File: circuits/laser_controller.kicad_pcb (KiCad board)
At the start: 4 copper layers, 173 x 61.1 mm, 180 parts, among them J1 USB_MINI_B, J2 USB_MINI_B, J5 24V DC IN, J6 CONN_RJ45, Q1 SOT-23, Q2 SOT-23, Q3 SOT-23, Q4 SOT-23, Q5 SOT-23, Q6 SOT-23, SW1 SW_PUSH, SW2 SW_PUSH, SW3 SW_PUSH, U1 SOIC-8_3.9x4.9mm_P1.27mm, U10 QFN-28-1EP_5x5mm_P0.5mm_EP3.3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, U11 SOT-23-5, U12 TSSOP-14_4.4x5mm_P0.65mm, U13 SOT-23, U14 LQFP-64_10x10mm_P0.5mm, U15 TSOT-23-6, U16 TSOT-23-6, U2 SOIC-8_3.9x4.9mm_P1.27mm, U3 SOIC-8_3.9x4.9mm_P1.27mm, U4 SOIC-8_3.9x4.9mm_P1.27mm, U5 SOT-23-5, U6 SOT-23-5, U7 SOT-23-5, U8 SOT-23-5, U9 ESP32-S3-WROOM-1

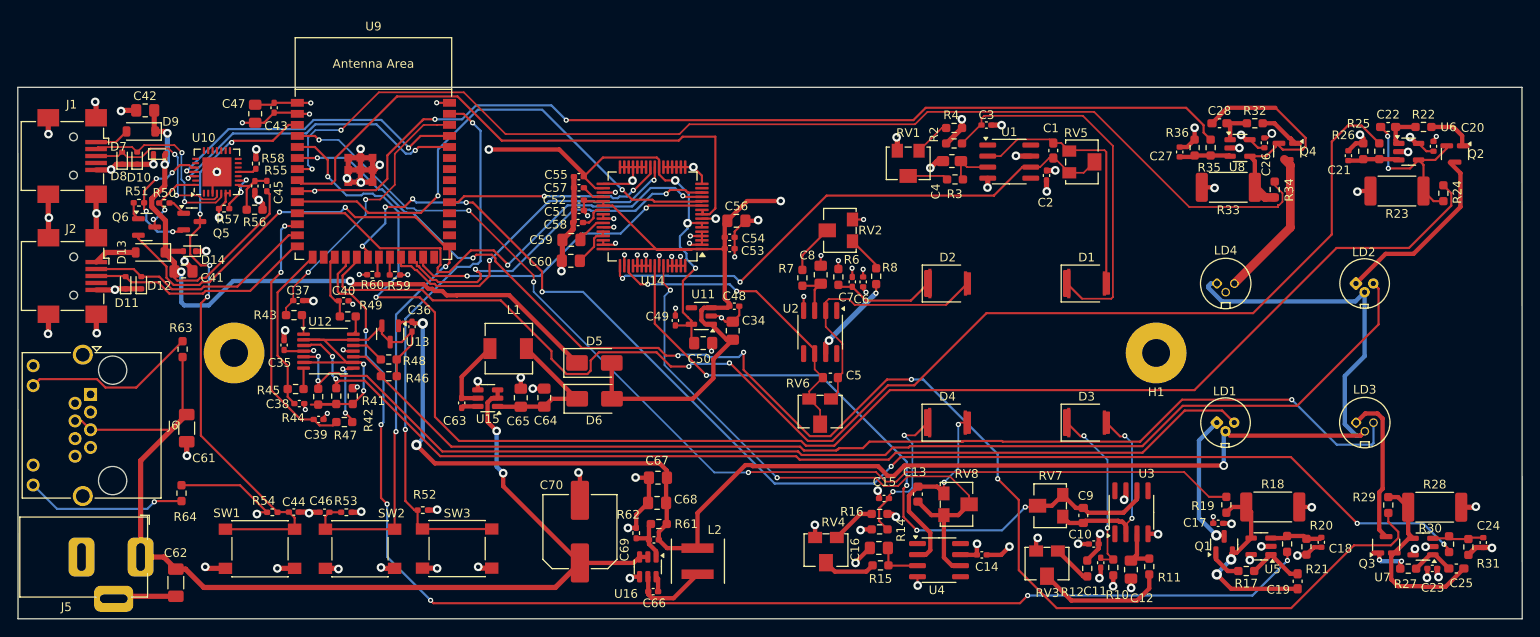
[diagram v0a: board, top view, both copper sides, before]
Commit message: Label laser controller board sections
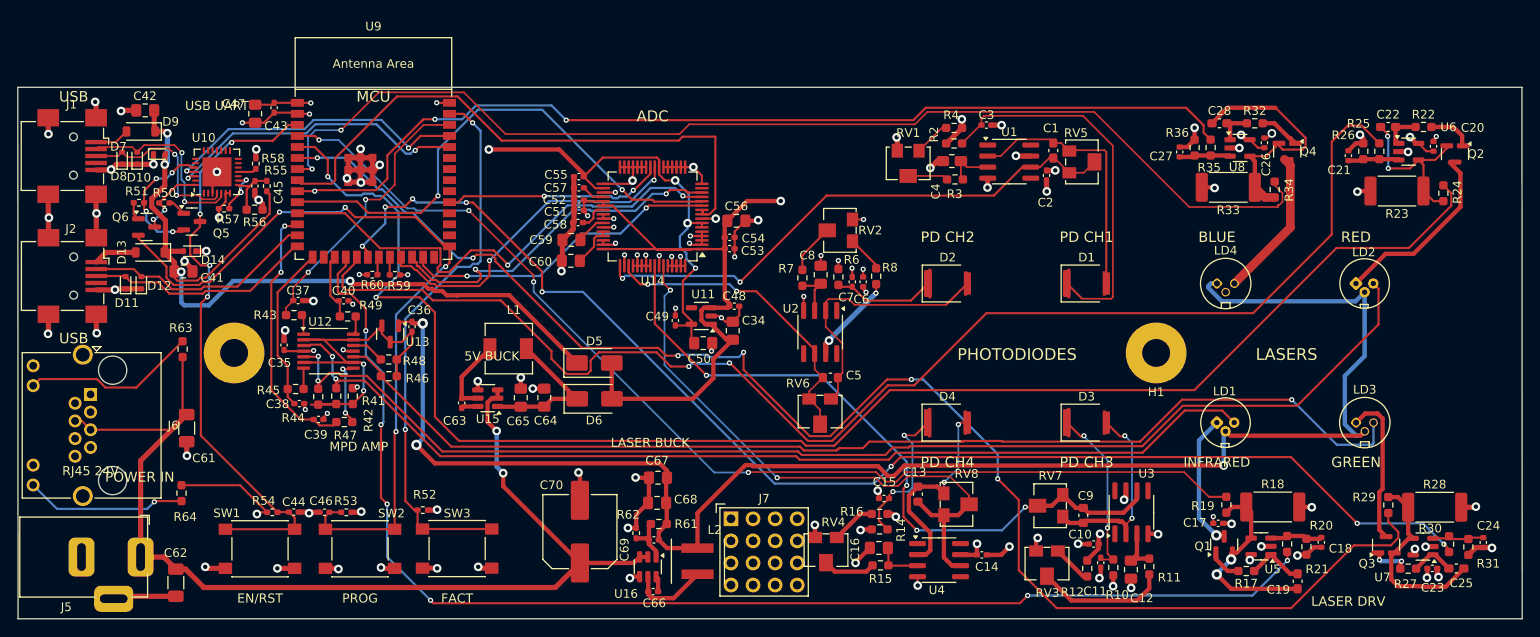
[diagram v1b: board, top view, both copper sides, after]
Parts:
- added J7: UTILITY_4X4, PinHeader_4x04_P2.54mm_Vertical, F.Cu at (113.0, 129.5)
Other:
- board text added: "5V BUCK"
- board text added: "ADC"
- board text added: "BLUE"
- board text added: "EN/RST"
- board text added: "FACT"
- board text added: "GREEN"
- board text added: "INFRARED"
- board text added: "LASER BUCK"
- board text added: "LASER DRV"
- board text added: "LASERS"
- board text added: "MCU"
- board text added: "MPD AMP"
- board text added: "PD CH1"
- board text added: "PD CH2"
- board text added: "PD CH3"
- board text added: "PD CH4"
- board text added: "PHOTODIODES"
- board text added: "POWER IN"
- board text added: "PROG"
- board text added: "RED"
- board text added: "RJ45 24V"
- board text added: "USB"
- board text added: "USB UART"
- board text added: "vivonics"
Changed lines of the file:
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@@
+    )
+  )
+  (footprint "PinHeader_4x04_P2.54mm_Vertical" (layer "F.Cu")
+    (at 113 129.5)
+    (descr "Through hole straight pin header, 4x04, 2.54mm pitch, vertical")
+    (tags "Through hole pin header THT 4x04 2.54mm vertical")
+    (attr through_hole)
+    (fp_text reference "J7" (at 3.81 -2.33) (layer "F.SilkS")
+        (effects (font (size 1 1) (thickness 0.15)))
+    )
+    (fp_text value "UTILITY_4X4" (at 3.81 9.95) (layer "F.Fab")
+        (effects (font (size 1 1) (thickness 0.15)))
+    )
+    (fp_text user "${REFERENCE}" (at 3.81 3.81) (layer "F.Fab")
+        (effects (font (size 1 1) (thickness 0.15)))
+    )
+    (fp_line (start -1.27 -1.27) (end 8.89 -1.27)
+      (stroke (width 0.12) (type solid)) (layer "F.SilkS"))
+    (fp_line (start -1.27 -1.27) (end -1.27 8.89)
+      (stroke (width 0.12) (type solid)) (layer "F.SilkS"))
+    (fp_line (start -1.27 8.89) (end 8.89 8.89)
+      (stroke (width 0.12) (type solid)) (layer "F.SilkS"))
+    (fp_line (start 8.89 -1.27) (end 8.89 8.89)
+      (stroke (width 0.12) (type solid)) (layer "F.SilkS"))
+    (fp_line (start -1.7 -1.7) (end -0.7 -1.7)
+      (stroke (width 0.12) (type solid)) (layer "F.SilkS"))
+    (fp_line (start -1.7 -1.7) (end -1.7 -0.7)
+      (stroke (width 0.12) (type solid)) (layer "F.SilkS"))
+    (fp_line (start -1.8 -1.8) (end 9.42 -1.8)
+      (stroke (width 0.05) (type solid)) (layer "F.CrtYd"))
+    (fp_line (start -1.8 9.42) (end -1.8 -1.8)
+      (stroke (width 0.05) (type solid)) (layer "F.CrtYd"))
+    (fp_line (start 9.42 -1.8) (end 9.42 9.42)
+      (stroke (width 0.05) (type solid)) (layer "F.CrtYd"))
+    (fp_line (start 9.42 9.42) (end -1.8 9.42)
+      (stroke (width 0.05) (type solid)) (layer "F.CrtYd"))
+    (fp_line (start -1.27 -0.27) (end -0.27 -1.27)
+      (stroke (width 0.1) (type solid)) (layer "F.Fab"))
+    (fp_line (start -1.27 -0.27) (end -1.27 8.89)
+      (stroke (width 0.1) (type solid)) (layer "F.Fab"))
+    (fp_line (start -1.27 8.89) (end 8.89 8.89)
+      (stroke (width 0.1) (type solid)) (layer "F.Fab"))
+    (fp_line (start -0.27 -1.27) (end 8.89 -1.27)
+      (stroke (width 0.1) (type solid)) (layer "F.Fab"))
+    (fp_line (start 8.89 -1.27) (end 8.89 8.89)
+      (stroke (width 0.1) (type solid)) (layer "F.Fab"))
+    (pad "1" thru_hole rect (at 0 0) (size 1.7 1.7) (drill 1) (layers "*.Cu" "*.Mask")
+      (net 46 "GND"))
+    (pad "2" thru_hole circle (at 2.54 0) (size 1.7 1.7) (drill 1) (layers "*.Cu" "*.Mask")
+      (net 115 "VIN_24V"))
+    (pad "3" thru_hole circle (at 5.08 0) (size 1.7 1.7) (drill 1) (layers "*.Cu" "*.Mask")
+      (net 2 "+5V"))
+    (pad "4" thru_hole circle (at 7.62 0) (size 1.7 1.7) (drill 1) (layers "*.Cu" "*.Mask")
+      (net 1 "+3V3"))
+    (pad "5" thru_hole circle (at 0 2.54) (size 1.7 1.7) (drill 1) (layers "*.Cu" "*.Mask")
+      (net 110 "PWM1"))
+    (pad "6" thru_hole circle (at 2.54 2.54) (size 1.7 1.7) (drill 1) (layers "*.Cu" "*.Mask")
+      (net 111 "PWM2"))
+    (pad "7" thru_hole circle (at 5.08 2.54) (size 1.7 1.7) (drill 1) (layers "*.Cu" "*.Mask")
+      (net 112 "PWM3"))
+    (pad "8" thru_hole circle (at 7.62 2.54) (size 1.7 1.7) (drill 1) (layers "*.Cu" "*.Mask")
+      (net 113 "PWM4"))
+    (pad "9" thru_hole circle (at 0 5.08) (size 1.7 1.7) (drill 1) (layers "*.Cu" "*.Mask")
+      (net 56 "MPD1"))
+    (pad "10" thru_hole circle (at 2.54 5.08) (size 1.7 1.7) (drill 1) (layers "*.Cu" "*.Mask")
+      (net 57 "MPD2"))
+    (pad "11" thru_hole circle (at 5.08 5.08) (size 1.7 1.7) (drill 1) (layers "*.Cu" "*.Mask")
+      (net 58 "MPD3"))
+    (pad "12" thru_hole circle (at 7.62 5.08) (size 1.7 1.7) (drill 1) (layers "*.Cu" "*.Mask")
+      (net 59 "MPD4"))
+    (pad "13" thru_hole circle (at 0 7.62) (size 1.7 1.7) (drill 1) (layers "*.Cu" "*.Mask")
+      (net 45 "CONVST"))
+    (pad "14" thru_hole circle (at 2.54 7.62) (size 1.7 1.7) (drill 1) (layers "*.Cu" "*.Mask")
+      (net 39 "ADC_BUSY"))
+    (pad "15" thru_hole circle (at 5.08 7.62) (size 1.7 1.7) (drill 1) (layers "*.Cu" "*.Mask")
+      (net 14 "/MCU_ESP32-S3/EN"))
+    (pad "16" thru_hole circle (at 7.62 7.62) (size 1.7 1.7) (drill 1) (layers "*.Cu" "*.Mask")
+      (net 31 "/MCU_ESP32-S3/PROG"))
+    (model "${KIPRJMOD}/packages3d/Connector_PinHeader.3dshapes/PinHeader_4x04_P2.54mm_Vertical.step"
+      (offset (xyz 0 0 0))
+      (scale (xyz 1 1 1))
+      (rotate (xyz 0 0 0))
     )
   )
@@
     (effects (font (size 1.2 1.2) (thickness 0.18)))
   )
+  (gr_text "PD CH2" (at 137.925 97.1 0) (layer "F.SilkS")
+    (effects (font (size 1.2 1.2) (thickness 0.18)))
+  )
+  (gr_text "PD CH1" (at 153.9 97.1 0) (layer "F.SilkS")
+    (effects (font (size 1.2 1.2) (thickness 0.18)))
+  )
+  (gr_text "BLUE" (at 168.9 97.1 0) (layer "F.SilkS")
+    (effects (font (size 1.2 1.2) (thickness 0.18)))
+  )
+  (gr_text "RED" (at 184.88 97.1 0) (layer "F.SilkS")
+    (effects (font (size 1.2 1.2) (thickness 0.18)))
+  )
+  (gr_text "PD CH4" (at 137.9 123 0) (layer "F.SilkS")
+    (effects (font (size 1.2 1.2) (thickness 0.18)))
+  )
+  (gr_text "PD CH3" (at 153.9 123 0) (layer "F.SilkS")
+    (effects (font (size 1.2 1.2) (thickness 0.18)))
+  )
+  (gr_text "INFRARED" (at 168.88 123 0) (layer "F.SilkS")
+    (effects (font (size 1.1 1.1) (thickness 0.17)))
+  )
+  (gr_text "GREEN" (at 184.9 123 0) (layer "F.SilkS")
+    (effects (font (size 1.2 1.2) (thickness 0.18)))
+  )
+  (gr_text "PHOTODIODES" (at 145.9 110.6 0) (layer "F.SilkS")
+    (effects (font (size 1.35 1.35) (thickness 0.22)))
+  )
+  (gr_text "LASERS" (at 176.9 110.6 0) (layer "F.SilkS")
+    (effects (font (size 1.35 1.35) (thickness 0.22)))
+  )
+  (gr_text "EN/RST" (at 58.8325 138.65 0) (layer "F.SilkS")
+    (effects (font (size 1.05 1.05) (thickness 0.16)))
+  )
+  (gr_text "PROG" (at 70.3325 138.65 0) (layer "F.SilkS")
+    (effects (font (size 1.05 1.05) (thickness 0.16)))
+  )
+  (gr_text "FACT" (at 81.5025 138.65 0) (layer "F.SilkS")
+    (effects (font (size 1.05 1.05) (thickness 0.16)))
+  )
+  (gr_text "USB" (at 37.4 80.95 0) (layer "F.SilkS")
+    (effects (font (size 1.2 1.2) (thickness 0.18)))
+  )
+  (gr_text "USB" (at 37.4 108.75 0) (layer "F.SilkS")
+    (effects (font (size 1.2 1.2) (thickness 0.18)))
+  )
+  (gr_text "RJ45 24V" (at 39.34 124 0) (layer "F.SilkS")
+    (effects (font (size 1.05 1.05) (thickness 0.16)))
+  )
+  (gr_text "POWER IN" (at 45 124.7 0) (layer "F.SilkS")
+    (effects (font (size 1.15 1.15) (thickness 0.18)))
+  )
+  (gr_text "MCU" (at 71.875 80.95 0) (layer "F.SilkS")
+    (effects (font (size 1.25 1.25) (thickness 0.2)))
+  )
+  (gr_text "USB UART" (at 53.875 82 0) (layer "F.SilkS")
+    (effects (font (size 1.05 1.05) (thickness 0.16)))
+  )
+  (gr_text "ADC" (at 103.9825 83.2 0) (layer "F.SilkS")
+    (effects (font (size 1.25 1.25) (thickness 0.2)))
+  )
+  (gr_text "MPD AMP" (at 70.2 121.2 0) (layer "F.SilkS")
+    (effects (font (size 1.05 1.05) (thickness 0.16)))
+  )
+  (gr_text "5V BUCK" (at 85.5 110.8 0) (layer "F.SilkS")
+    (effects (font (size 1.05 1.05) (thickness 0.16)))
+  )
+  (gr_text "LASER BUCK" (at 103.7 120.75 0) (layer "F.SilkS")
+    (effects (font (size 1.05 1.05) (thickness 0.16)))
+  )
+  (gr_text "LASER DRV" (at 184 139 0) (layer "F.SilkS")
+    (effects (font (size 1.1 1.1) (thickness 0.17)))
+  )
+  (gr_text "vivonics" (at 117.5 111 0) (layer "B.SilkS")
+    (effects (font (size 12 12) (thickness 1.4)) (justify mirror))
+  )
   (segment (start 60.4542 82.7883) (end 62.9883 82.7883) (width 0.25) (layer "F.Cu") (net 1))

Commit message: Use SMT 4x2 utility header
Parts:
- J7: value UTILITY_4X4 -> C192300; footprint PinHeader_4x04_P2.54mm_Vertical -> PinHeader_2x04_P2.54mm_SMD_Vertical_C192300
- moved J7 0.50 mm to (112.5, 129.5)
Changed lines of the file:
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@@
     )
   )
-  (footprint "PinHeader_4x04_P2.54mm_Vertical" (layer "F.Cu")
-    (at 113 129.5)
-    (descr "Through hole straight pin header, 4x04, 2.54mm pitch, vertical")
-    (tags "Through hole pin header THT 4x04 2.54mm vertical")
-    (attr through_hole)
-    (fp_text reference "J7" (at 3.81 -2.33) (layer "F.SilkS")
+  (footprint "PinHeader_2x04_P2.54mm_SMD_Vertical_C192300" (layer "F.Cu")
+    (at 112.5 129.5)
+    (descr "BOOMELE 2.54-2*4P, LCSC C192300, 2x4 2.54mm pitch SMT vertical pin header")
+    (tags "C192300 BOOMELE 2.54-2*4P SMT SMD pin header")
+    (attr smd)
+    (fp_text reference "J7" (at 3.81 -2.1) (layer "F.SilkS")
         (effects (font (size 1 1) (thickness 0.15)))
     )
-    (fp_text value "UTILITY_4X4" (at 3.81 9.95) (layer "F.Fab")
+    (fp_text value "C192300" (at 3.81 4.8) (layer "F.Fab")
         (effects (font (size 1 1) (thickness 0.15)))
     )
-    (fp_text user "${REFERENCE}" (at 3.81 3.81) (layer "F.Fab")
+    (fp_text user "${REFERENCE}" (at 3.81 1.27) (layer "F.Fab")
         (effects (font (size 1 1) (thickness 0.15)))
     )
-    (fp_line (start -1.27 -1.27) (end 8.89 -1.27)
+    (fp_text user "C192300" (at 3.81 3.65) (layer "F.Fab")
+        (effects (font (size 0.8 0.8) (thickness 0.12)))
+    )
+    (fp_line (start -1.2 -1.2) (end 8.82 -1.2)
       (stroke (width 0.12) (type solid)) (layer "F.SilkS"))
-    (fp_line (start -1.27 -1.27) (end -1.27 8.89)
+    (fp_line (start -1.2 -1.2) (end -1.2 3.74)
       (stroke (width 0.12) (type solid)) (layer "F.SilkS"))
-    (fp_line (start -1.27 8.89) (end 8.89 8.89)
+    (fp_line (start -1.2 3.74) (end 8.82 3.74)
       (stroke (width 0.12) (type solid)) (layer "F.SilkS"))
-    (fp_line (start 8.89 -1.27) (end 8.89 8.89)
+    (fp_line (start 8.82 -1.2) (end 8.82 3.74)
       (stroke (width 0.12) (type solid)) (layer "F.SilkS"))
     (fp_line (start -1.7 -1.7) (end -0.7 -1.7)
@@
     (fp_line (start -1.7 -1.7) (end -1.7 -0.7)
       (stroke (width 0.12) (type solid)) (layer "F.SilkS"))
-    (fp_line (start -1.8 -1.8) (end 9.42 -1.8)
+    (fp_line (start -1.9 -1.9) (end 9.52 -1.9)
       (stroke (width 0.05) (type solid)) (layer "F.CrtYd"))
-    (fp_line (start -1.8 9.42) (end -1.8 -1.8)
+    (fp_line (start -1.9 4.44) (end -1.9 -1.9)
       (stroke (width 0.05) (type solid)) (layer "F.CrtYd"))
-    (fp_line (start 9.42 -1.8) (end 9.42 9.42)
+    (fp_line (start 9.52 -1.9) (end 9.52 4.44)
       (stroke (width 0.05) (type solid)) (layer "F.CrtYd"))
-    (fp_line (start 9.42 9.42) (end -1.8 9.42)
+    (fp_line (start 9.52 4.44) (end -1.9 4.44)
       (stroke (width 0.05) (type solid)) (layer "F.CrtYd"))
-    (fp_line (start -1.27 -0.27) (end -0.27 -1.27)
+    (fp_line (start -1.2 -0.2) (end -0.2 -1.2)
       (stroke (width 0.1) (type solid)) (layer "F.Fab"))
-    (fp_line (start -1.27 -0.27) (end -1.27 8.89)
+    (fp_line (start -1.2 -0.2) (end -1.2 3.74)
       (stroke (width 0.1) (type solid)) (layer "F.Fab"))
-    (fp_line (start -1.27 8.89) (end 8.89 8.89)
+    (fp_line (start -1.2 3.74) (end 8.82 3.74)
       (stroke (width 0.1) (type solid)) (layer "F.Fab"))
-    (fp_line (start -0.27 -1.27) (end 8.89 -1.27)
+    (fp_line (start -0.2 -1.2) (end 8.82 -1.2)
       (stroke (width 0.1) (type solid)) (layer "F.Fab"))
-    (fp_line (start 8.89 -1.27) (end 8.89 8.89)
+    (fp_line (start 8.82 -1.2) (end 8.82 3.74)
       (stroke (width 0.1) (type solid)) (layer "F.Fab"))
-    (pad "1" thru_hole rect (at 0 0) (size 1.7 1.7) (drill 1) (layers "*.Cu" "*.Mask")
+    (pad "1" smd roundrect (at 0 0) (size 1.6 1.8) (layers "F.Cu" "F.Paste" "F.Mask") (roundrect_rratio 0.15)
       (net 46 "GND"))
-    (pad "2" thru_hole circle (at 2.54 0) (size 1.7 1.7) (drill 1) (layers "*.Cu" "*.Mask")
+    (pad "2" smd roundrect (at 2.54 0) (size 1.6 1.8) (layers "F.Cu" "F.Paste" "F.Mask") (roundrect_rratio 0.15)
       (net 115 "VIN_24V"))
-    (pad "3" thru_hole circle (at 5.08 0) (size 1.7 1.7) (drill 1) (layers "*.Cu" "*.Mask")
+    (pad "3" smd roundrect (at 5.08 0) (size 1.6 1.8) (layers "F.Cu" "F.Paste" "F.Mask") (roundrect_rratio 0.15)
       (net 2 "+5V"))
-    (pad "4" thru_hole circle (at 7.62 0) (size 1.7 1.7) (drill 1) (layers "*.Cu" "*.Mask")
+    (pad "4" smd roundrect (at 7.62 0) (size 1.6 1.8) (layers "F.Cu" "F.Paste" "F.Mask") (roundrect_rratio 0.15)
       (net 1 "+3V3"))
-    (pad "5" thru_hole circle (at 0 2.54) (size 1.7 1.7) (drill 1) (layers "*.Cu" "*.Mask")
+    (pad "5" smd roundrect (at 0 2.54) (size 1.6 1.8) (layers "F.Cu" "F.Paste" "F.Mask") (roundrect_rratio 0.15)
       (net 110 "PWM1"))
-    (pad "6" thru_hole circle (at 2.54 2.54) (size 1.7 1.7) (drill 1) (layers "*.Cu" "*.Mask")
+    (pad "6" smd roundrect (at 2.54 2.54) (size 1.6 1.8) (layers "F.Cu" "F.Paste" "F.Mask") (roundrect_rratio 0.15)
       (net 111 "PWM2"))
-    (pad "7" thru_hole circle (at 5.08 2.54) (size 1.7 1.7) (drill 1) (layers "*.Cu" "*.Mask")
+    (pad "7" smd roundrect (at 5.08 2.54) (size 1.6 1.8) (layers "F.Cu" "F.Paste" "F.Mask") (roundrect_rratio 0.15)
       (net 112 "PWM3"))
-    (pad "8" thru_hole circle (at 7.62 2.54) (size 1.7 1.7) (drill 1) (layers "*.Cu" "*.Mask")
+    (pad "8" smd roundrect (at 7.62 2.54) (size 1.6 1.8) (layers "F.Cu" "F.Paste" "F.Mask") (roundrect_rratio 0.15)
       (net 113 "PWM4"))
-    (pad "9" thru_hole circle (at 0 5.08) (size 1.7 1.7) (drill 1) (layers "*.Cu" "*.Mask")
-      (net 56 "MPD1"))
-    (pad "10" thru_hole circle (at 2.54 5.08) (size 1.7 1.7) (drill 1) (layers "*.Cu" "*.Mask")
-      (net 57 "MPD2"))
-    (pad "11" thru_hole circle (at 5.08 5.08) (size 1.7 1.7) (drill 1) (layers "*.Cu" "*.Mask")
-      (net 58 "MPD3"))
-    (pad "12" thru_hole circle (at 7.62 5.08) (size 1.7 1.7) (drill 1) (layers "*.Cu" "*.Mask")
-      (net 59 "MPD4"))
-    (pad "13" thru_hole circle (at 0 7.62) (size 1.7 1.7) (drill 1) (layers "*.Cu" "*.Mask")
-      (net 45 "CONVST"))
-    (pad "14" thru_hole circle (at 2.54 7.62) (size 1.7 1.7) (drill 1) (layers "*.Cu" "*.Mask")
-      (net 39 "ADC_BUSY"))
-    (pad "15" thru_hole circle (at 5.08 7.62) (size 1.7 1.7) (drill 1) (layers "*.Cu" "*.Mask")
-      (net 14 "/MCU_ESP32-S3/EN"))
-    (pad "16" thru_hole circle (at 7.62 7.62) (size 1.7 1.7) (drill 1) (layers "*.Cu" "*.Mask")
-      (net 31 "/MCU_ESP32-S3/PROG"))
-    (model "${KIPRJMOD}/packages3d/Connector_PinHeader.3dshapes/PinHeader_4x04_P2.54mm_Vertical.step"
+    (model "${KIPRJMOD}/packages3d/Connector_PinHeader.3dshapes/PinHeader_2x04_P2.54mm_SMD_Vertical_C192300.step"
       (offset (xyz 0 0 0))
       (scale (xyz 1 1 1))
